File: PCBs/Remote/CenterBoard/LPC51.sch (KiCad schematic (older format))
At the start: 24 parts, among them J201 DX07S016JA1R1500, U201 LPC51U68JBD64, U202 W25Q128JVS

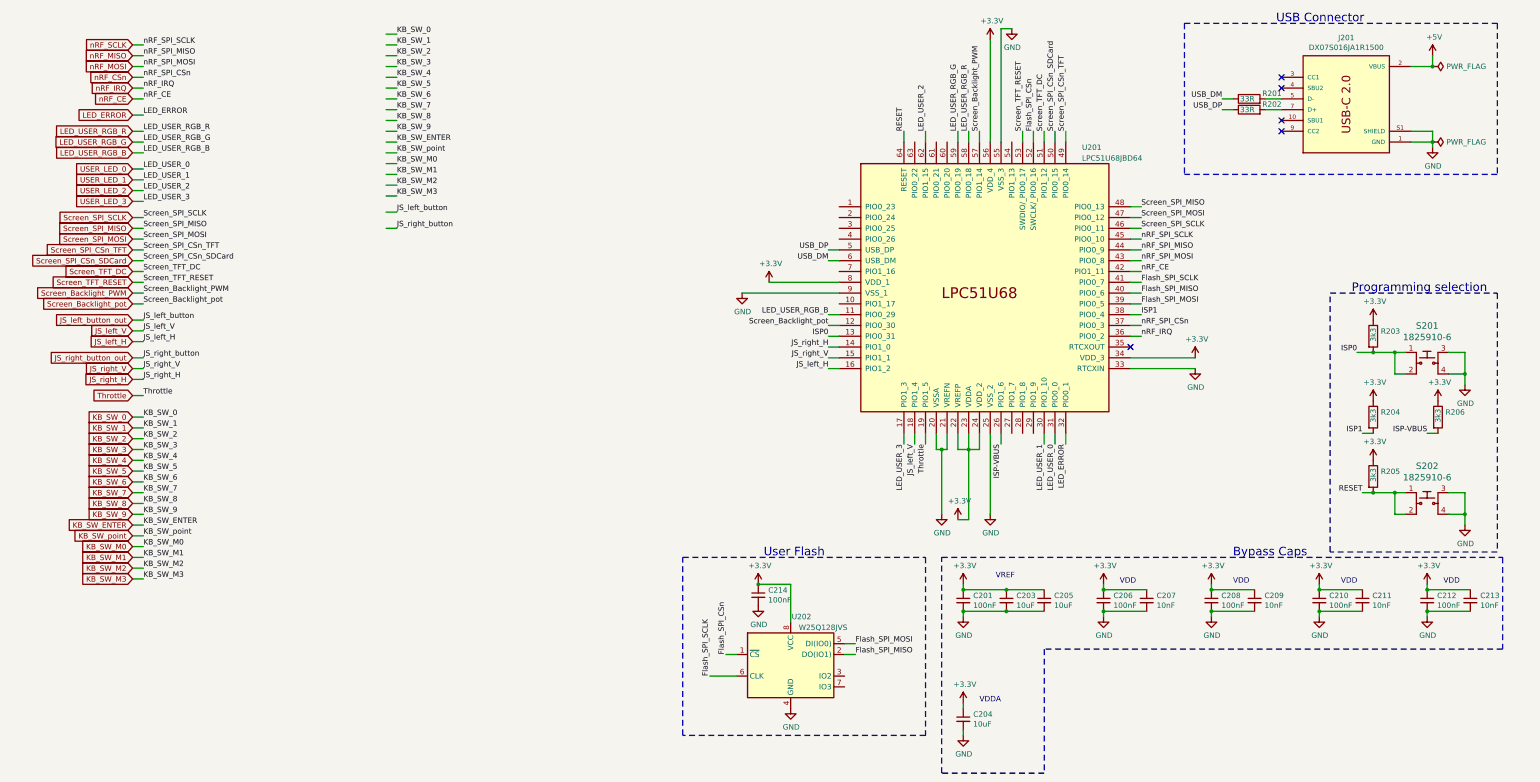
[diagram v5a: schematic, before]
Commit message: Finished leds, redid a lot of PCB wiring. Almost done there now.
Signed-off-by: Eldalote.Electronics <Eldalote.Electronics@gmail.com>
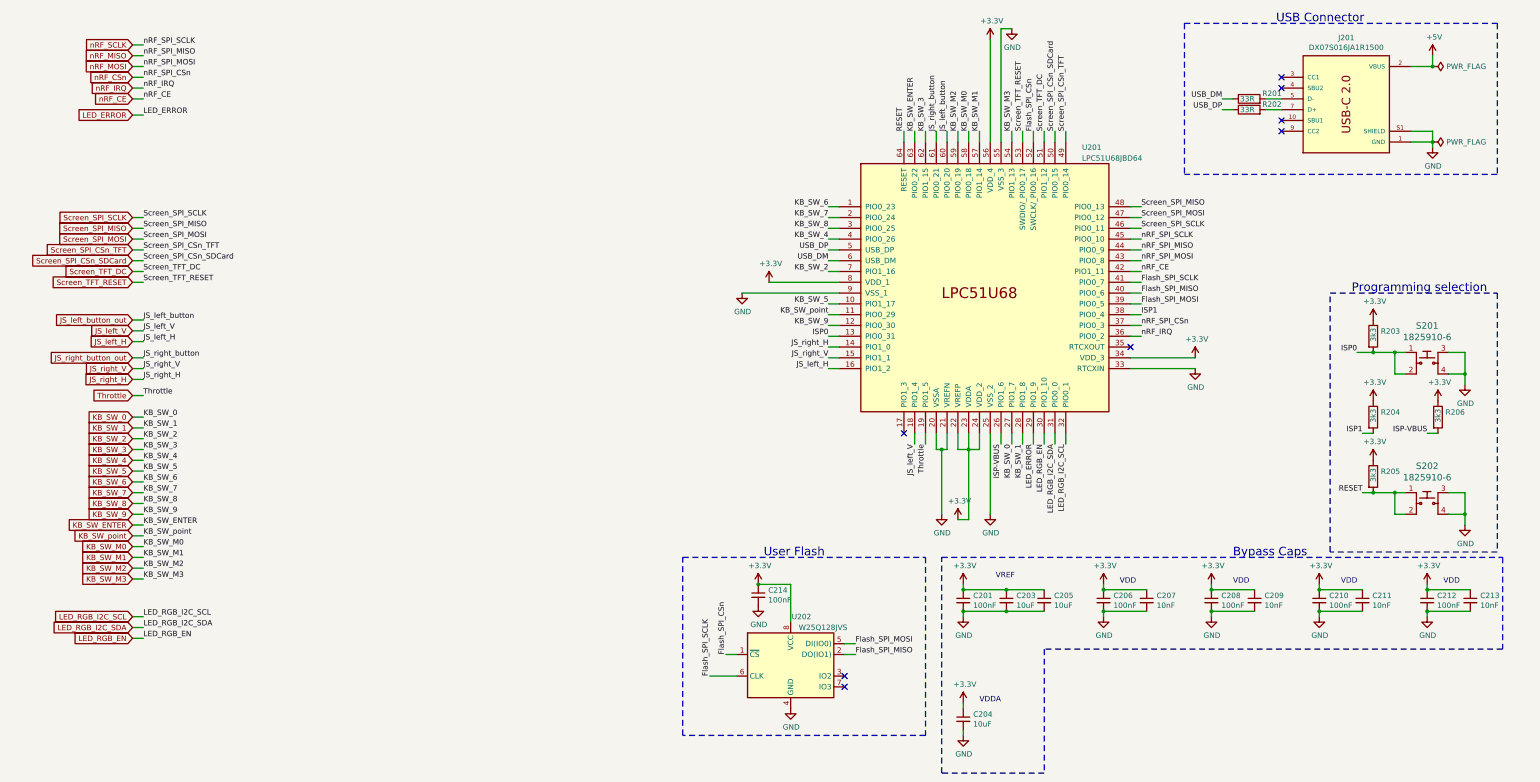
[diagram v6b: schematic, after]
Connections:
- net labels added: LED_RGB_EN, LED_RGB_I2C_SCL, LED_RGB_I2C_SDA
- net labels removed: LED_USER_0, LED_USER_1, LED_USER_2, LED_USER_3, LED_USER_RGB_B, LED_USER_RGB_G, LED_USER_RGB_R, Screen_Backlight_PWM, Screen_Backlight_pot, USER_LED_0, USER_LED_1, USER_LED_2, USER_LED_3
- wire segments 182 -> 170
- no-connect marks 5 -> 8
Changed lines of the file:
@@
 	-1550 1200 -1450 1200
 Wire Wire Line
-	-1450 3200 -1550 3200
-Text Label -1450 3200 0    50   ~ 0
-Screen_Backlight_pot
-Wire Wire Line
 	-1550 2400 -1450 2400
 Wire Wire Line
@@
 Wire Wire Line
 	-1550 2800 -1450 2800
-Wire Wire Line
-	-1550 3100 -1450 3100
 Text Label -1450 2400 0    50   ~ 0
 Screen_SPI_SCLK
@@
 Text Label -1450 2800 0    50   ~ 0
 Screen_SPI_CSn_SDCard
-Text Label -1450 3100 0    50   ~ 0
-Screen_Backlight_PWM
 Text GLabel -1550 1450 0    50   Input ~ 0
 LED_ERROR
-Text GLabel -1550 1600 0    50   Input ~ 0
-LED_USER_RGB_R
-Text GLabel -1550 1700 0    50   Input ~ 0
-LED_USER_RGB_G
-Text GLabel -1550 1800 0    50   Input ~ 0
-LED_USER_RGB_B
-Text GLabel -1550 1950 0    50   Input ~ 0
-USER_LED_0
-Text GLabel -1550 2050 0    50   Input ~ 0
-USER_LED_1
-Text GLabel -1550 2150 0    50   Input ~ 0
-USER_LED_2
-Text GLabel -1550 2250 0    50   Input ~ 0
-USER_LED_3
 Text GLabel -1550 2400 0    50   Input ~ 0
 Screen_SPI_SCLK
@@
 Text GLabel -1550 3000 0    50   Input ~ 0
 Screen_TFT_RESET
-Text GLabel -1550 3100 0    50   Input ~ 0
-Screen_Backlight_PWM
-Text GLabel -1550 3200 0    50   Input ~ 0
-Screen_Backlight_pot
 Wire Wire Line
 	-1550 3350 -1450 3350
@@
 nRF_CE
 Wire Wire Line
-	4900 3400 5000 3400
-Text Label 4900 3400 2    50   ~ 0
-Screen_Backlight_pot
-Wire Wire Line
 	7700 2500 7800 2500
 Wire Wire Line
@@
 Wire Wire Line
 	7000 1700 7000 1600
-Wire Wire Line
-	6300 1700 6300 1600
 Text Label 7800 2500 0    50   ~ 0
 Screen_SPI_SCLK
@@
 Text Label 7000 1600 1    50   ~ 0
 Screen_SPI_CSn_SDCard
-Text Label 6300 1600 1    50   ~ 0
-Screen_Backlight_PWM
 Wire Wire Line
 	7800 3200 7700 3200
@@
 Text Label -1450 1300 0    50   ~ 0
 nRF_CE
-Text Label -1450 2250 0    50   ~ 0
-LED_USER_3
-Text Label -1450 2150 0    50   ~ 0
-LED_USER_2
-Text Label -1450 2050 0    50   ~ 0
-LED_USER_1
-Text Label -1450 1950 0    50   ~ 0
-LED_USER_0
-Wire Wire Line
-	-1450 2250 -1550 2250
-Wire Wire Line
-	-1450 2150 -1550 2150
-Wire Wire Line
-	-1450 2050 -1550 2050
-Wire Wire Line
-	-1450 1950 -1550 1950
-Text Label -1450 1600 0    50   ~ 0
-LED_USER_RGB_R
-Text Label -1450 1700 0    50   ~ 0
-LED_USER_RGB_G
-Text Label -1450 1800 0    50   ~ 0
-LED_USER_RGB_B
-Wire Wire Line
-	-1450 1600 -1550 1600
-Wire Wire Line
-	-1450 1700 -1550 1700
-Wire Wire Line
-	-1550 1800 -1450 1800
 Text Label -1450 1450 0    50   ~ 0
 LED_ERROR
@@
 Wire Wire Line
 	-1550 1300 -1450 1300
-Text Label 5600 4500 3    50   ~ 0
-LED_USER_3
-Text Label 5800 1600 1    50   ~ 0
-LED_USER_2
-Text Label 6900 4500 3    50   ~ 0
-LED_USER_1
-Text Label 7000 4500 3    50   ~ 0
-LED_USER_0
-Wire Wire Line
-	5600 4500 5600 4400
-Wire Wire Line
-	5800 1600 5800 1700
-Wire Wire Line
-	6900 4500 6900 4400
-Wire Wire Line
-	7000 4500 7000 4400
-Text Label 6200 1600 1    50   ~ 0
-LED_USER_RGB_R
-Text Label 6100 1600 1    50   ~ 0
-LED_USER_RGB_G
-Text Label 4900 3300 2    50   ~ 0
-LED_USER_RGB_B
-Wire Wire Line
-	6200 1600 6200 1700
-Wire Wire Line
-	6100 1600 6100 1700
-Wire Wire Line
-	5000 3300 4900 3300
-Text Label 7100 4500 3    50   ~ 0
-LED_ERROR
-Wire Wire Line
-	7100 4400 7100 4500
-Wire Wire Line
-	800  2350 900  2350
-Text Label 900  2350 0    50   ~ 0
+Wire Wire Line
+	5800 1700 5800 1600
+Text Label 6000 1600 1    50   ~ 0
 JS_left_button
 Wire Wire Line
@@
 JS_right_H
 Wire Wire Line
-	800  2500 900  2500
-Text Label 900  2500 0    50   ~ 0
+	5700 1700 5700 1600
+Text Label 5900 1600 1    50   ~ 0
 JS_right_button
 Wire Wire Line
@@
 KB_SW_M3
 Wire Wire Line
-	800  700  900  700
-Wire Wire Line
-	800  800  900  800
-Wire Wire Line
-	800  900  900  900
-Wire Wire Line
-	800  1000 900  1000
-Wire Wire Line
-	800  1100 900  1100
-Wire Wire Line
-	800  1200 900  1200
-Wire Wire Line
-	800  1300 900  1300
-Wire Wire Line
-	800  1400 900  1400
-Wire Wire Line
-	800  1500 900  1500
-Wire Wire Line
-	800  1600 900  1600
-Wire Wire Line
-	800  1700 900  1700
-Wire Wire Line
-	800  1800 900  1800
-Wire Wire Line
-	800  1900 900  1900
-Wire Wire Line
-	800  2000 900  2000
-Wire Wire Line
-	800  2100 900  2100
-Wire Wire Line
-	800  2200 900  2200
-Text Label 900  700  0    50   ~ 0
+	6600 4400 6600 4500
+Wire Wire Line
+	6700 4400 6700 4500
+Wire Wire Line
+	5000 2900 4900 2900
+Wire Wire Line
+	6200 1700 6200 1600
+Wire Wire Line
+	5000 2600 4900 2600
+Wire Wire Line
+	5000 3200 4900 3200
+Wire Wire Line
+	5000 2300 4900 2300
+Wire Wire Line
+	5000 2400 4900 2400
+Wire Wire Line
+	5000 2500 4900 2500
+Wire Wire Line
+	5000 3400 4900 3400
+Wire Wire Line
+	5900 1700 5900 1600
+Wire Wire Line
+	5000 3300 4900 3300
+Wire Wire Line
+	6100 1700 6100 1600
+Wire Wire Line
+	6300 1700 6300 1600
+Wire Wire Line
+	6000 1700 6000 1600
+Wire Wire Line
+	6600 1700 6600 1600
+Text Label 6600 4500 3    50   ~ 0
 KB_SW_0
-Text Label 900  800  0    50   ~ 0
+Text Label 6700 4500 3    50   ~ 0
 KB_SW_1
-Text Label 900  900  0    50   ~ 0
+Text Label 4900 2900 2    50   ~ 0
 KB_SW_2
-Text Label 900  1000 0    50   ~ 0
+Text Label 5800 1600 1    50   ~ 0
 KB_SW_3
-Text Label 900  1100 0    50   ~ 0
+Text Label 4900 2600 2    50   ~ 0
 KB_SW_4
-Text Label 900  1200 0    50   ~ 0
+Text Label 4900 3200 2    50   ~ 0
 KB_SW_5
-Text Label 900  1300 0    50   ~ 0
+Text Label 4900 2300 2    50   ~ 0
 KB_SW_6
-Text Label 900  1400 0    50   ~ 0
+Text Label 4900 2400 2    50   ~ 0
 KB_SW_7
-Text Label 900  1500 0    50   ~ 0
+Text Label 4900 2500 2    50   ~ 0
 KB_SW_8
-Text Label 900  1600 0    50   ~ 0
+Text Label 4900 3400 2    50   ~ 0
 KB_SW_9
-Text Label 900  1700 0    50   ~ 0
+Text Label 5700 1600 1    50   ~ 0
 KB_SW_ENTER
-Text Label 900  1800 0    50   ~ 0
+Text Label 4900 3300 2    50   ~ 0
 KB_SW_point
-Text Label 900  1900 0    50   ~ 0
+Text Label 6200 1600 1    50   ~ 0
 KB_SW_M0
-Text Label 900  2000 0    50   ~ 0
+Text Label 6300 1600 1    50   ~ 0
 KB_SW_M1
-Text Label 900  2100 0    50   ~ 0
+Text Label 6100 1600 1    50   ~ 0
 KB_SW_M2
-Text Label 900  2200 0    50   ~ 0
+Text Label 6600 1600 1    50   ~ 0
 KB_SW_M3
 Wire Notes Line
@@
 	1    0    0    -1
 $EndComp
+Wire Wire Line
+	-1550 6300 -1450 6300
+Wire Wire Line
+	-1450 6200 -1550 6200
+Wire Wire Line
+	-1450 6100 -1550 6100
+Text Label -1450 6300 0    50   ~ 0
+LED_RGB_EN
+Text Label -1450 6200 0    50   ~ 0
+LED_RGB_I2C_SDA
+Text Label -1450 6100 0    50   ~ 0
+LED_RGB_I2C_SCL
+Text GLabel -1550 6100 0    50   Input ~ 0
+LED_RGB_I2C_SCL
+Text GLabel -1550 6200 0    50   Input ~ 0
+LED_RGB_I2C_SDA
+Text GLabel -1550 6300 0    50   Input ~ 0
+LED_RGB_EN
+Wire Wire Line
+	6900 4400 6900 4500
+Wire Wire Line
+	7000 4500 7000 4400
+Wire Wire Line
+	7100 4500 7100 4400
+Text Label 6900 4500 3    50   ~ 0
+LED_RGB_EN
+Text Label 7000 4500 3    50   ~ 0
+LED_RGB_I2C_SDA
+Text Label 7100 4500 3    50   ~ 0
+LED_RGB_I2C_SCL
+Text Label 6800 4500 3    50   ~ 0
+LED_ERROR
+Wire Wire Line
+	6800 4400 6800 4500
+NoConn ~ 5600 4400
+NoConn ~ 5050 6650
+NoConn ~ 5050 6750
 $EndSCHEMATC

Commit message: More finishing work on remote-centerboard. Copied in the Drone main board, did some cleaning up on that. Started work on  more neat and clean lessons learned documents
Signed-off-by: Eldalote.Electronics <Eldalote.Electronics@gmail.com>
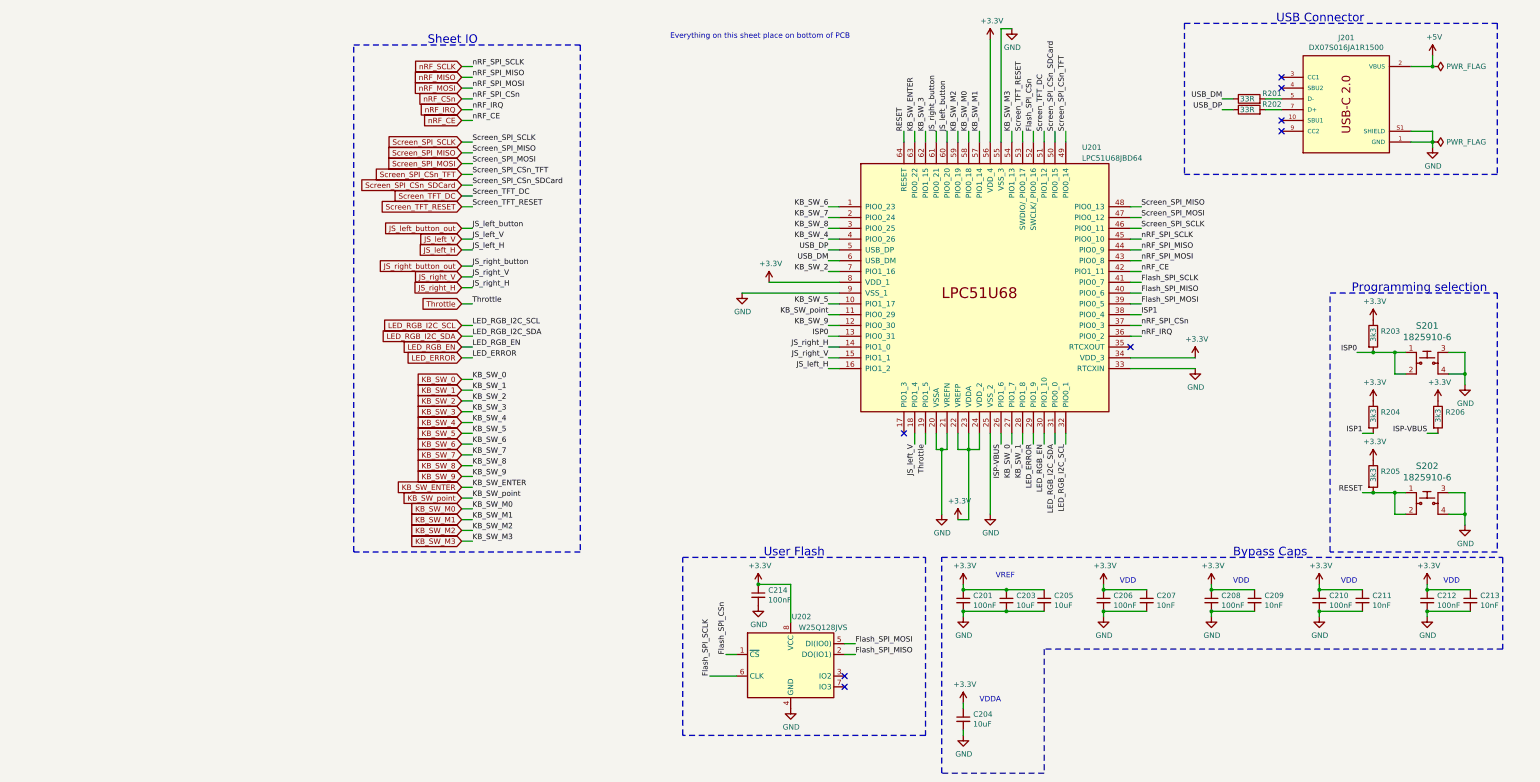
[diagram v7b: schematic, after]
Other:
- note added: "Everything on this sheet place on bottom of PCB"
- note added: "Sheet IO"
